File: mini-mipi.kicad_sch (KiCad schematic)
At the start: 0 parts

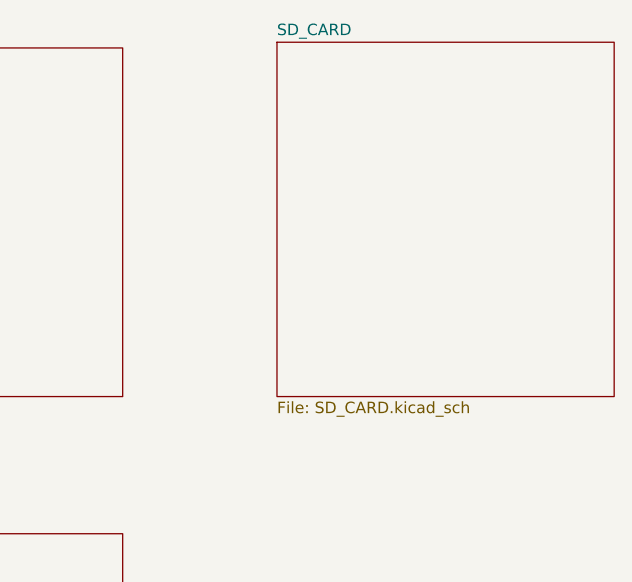
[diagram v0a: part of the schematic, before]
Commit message: Remove SD card, relocate regulators
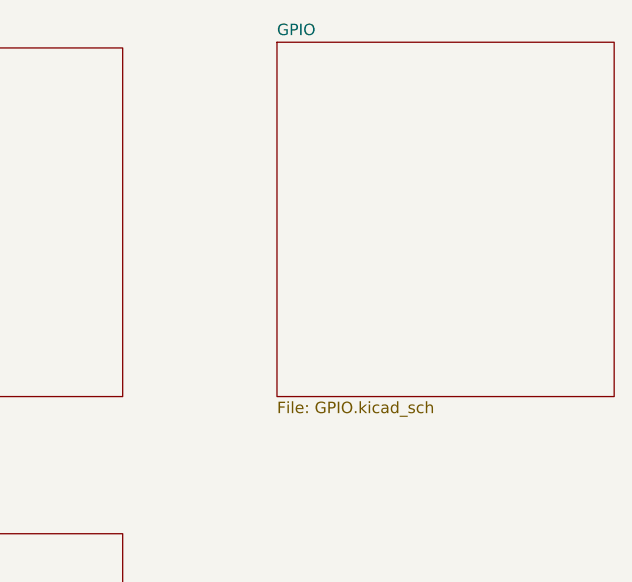
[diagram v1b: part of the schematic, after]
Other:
- sheet SD_CARD renamed GPIO
- sheet GPIO: file SD_CARD.kicad_sch -> GPIO.kicad_sch
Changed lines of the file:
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@@
-(kicad_sch (version 20200714) (host eeschema "5.99.0-unknown-8324cb3~102~ubuntu20.04.1")
+(kicad_sch (version 20200714) (host eeschema "5.99.0-unknown-027b6c8cf~102~ubuntu20.04.1")
   (page 1 6)
   (paper "A4")
@@
     )
   )
+  (sheet (at 207.645 43.18) (size 37.465 39.37)
+    (stroke (width 0.001) (type solid) (color 132 0 132 1))
+    (fill (color 255 255 255 0.0000))
+    (property "Sheet name" "GPIO" (id 0) (at 207.645 42.5441 0)
+      (effects (font (size 1.27 1.27)) (justify left bottom))
+    )
+    (property "Sheet file" "GPIO.kicad_sch" (id 1) (at 207.645 83.0589 0)
+      (effects (font (size 1.27 1.27)) (justify left top))
+    )
+  )
   (sheet (at 95.885 97.79) (size 34.925 29.845)
     (stroke (width 0.001) (type solid) (color 132 0 132 1))
@@
     )
   )
-  (sheet (at 207.645 43.18) (size 37.465 39.37)
-    (stroke (width 0.001) (type solid) (color 132 0 132 1))
-    (fill (color 255 255 255 0.0000))
-    (property "Sheet name" "SD_CARD" (id 0) (at 207.645 42.5441 0)
-      (effects (font (size 1.27 1.27)) (justify left bottom))
-    )
-    (property "Sheet file" "SD_CARD.kicad_sch" (id 1) (at 207.645 83.0589 0)
-      (effects (font (size 1.27 1.27)) (justify left top))
-    )
-  )
   (symbol_instances
     (path "/baa53bf9-daca-49ae-9e0d-ffb475a21435/898ad7f7-a0c6-4b72-8696-d86ef31c42ed"
@@
       (reference "#PWR0137") (unit 1)
     )
+    (path "/baa53bf9-daca-49ae-9e0d-ffb475a21435/310a54e5-8519-46fa-8e90-bd75a4f06582"
+      (reference "#PWR0151") (unit 1)
+    )
     (path "/baa53bf9-daca-49ae-9e0d-ffb475a21435/e369df8d-7bc0-4018-abea-2ddbb0b05648"
       (reference "C16") (unit 1)
@@
       (reference "C19") (unit 1)
     )
+    (path "/baa53bf9-daca-49ae-9e0d-ffb475a21435/9d904033-ab25-4a85-887c-bd0fbbf444d9"
+      (reference "C22") (unit 1)
+    )
     (path "/baa53bf9-daca-49ae-9e0d-ffb475a21435/70e6299b-b19c-469b-8113-15ef76301879"
       (reference "IC1") (unit 3)
@@
       (reference "#PWR0127") (unit 1)
     )
-    (path "/3f6b20e2-0af0-4e6d-a239-fbbb920f7ad3/efa53525-f126-4098-9bce-088c58985fd3"
+    (path "/3f6b20e2-0af0-4e6d-a239-fbbb920f7ad3/032a150b-85ae-4c68-ae3f-f4937bcc702e"
       (reference "#PWR0128") (unit 1)
     )
@@
       (reference "C2") (unit 1)
     )
-    (path "/3f6b20e2-0af0-4e6d-a239-fbbb920f7ad3/b2406567-d175-4f71-b4e4-c30e3317692d"
+    (path "/3f6b20e2-0af0-4e6d-a239-fbbb920f7ad3/b3910606-f8a0-414a-972a-a13f3f20bf6f"
       (reference "D1") (unit 1)
-    )
-    (path "/3f6b20e2-0af0-4e6d-a239-fbbb920f7ad3/4a8d2ba4-dd12-4599-94c3-38aad859b794"
-      (reference "D2") (unit 1)
     )
     (path "/3f6b20e2-0af0-4e6d-a239-fbbb920f7ad3/17ffadec-0811-496b-a0ce-0bdb99a7bf76"
@@
       (reference "R20") (unit 1)
     )
+    (path "/3f6b20e2-0af0-4e6d-a239-fbbb920f7ad3/b73fbf2e-397b-4acc-b296-438da13da3bd"
+      (reference "R25") (unit 1)
+    )
     (path "/3f6b20e2-0af0-4e6d-a239-fbbb920f7ad3/0f5c113f-b95a-4ea7-a5ce-136619995088"
       (reference "U5") (unit 1)
@@
       (reference "#PWR0143") (unit 1)
     )
+    (path "/8f541333-71c5-4e69-a5cb-3da6766b8bdb/e0b9767b-9f41-4b80-891c-0264532b6d01"
+      (reference "#PWR0144") (unit 1)
+    )
+    (path "/8f541333-71c5-4e69-a5cb-3da6766b8bdb/9f554b2f-50ba-43f3-8a86-bed4cf6888d8"
+      (reference "#PWR0145") (unit 1)
+    )
     (path "/8f541333-71c5-4e69-a5cb-3da6766b8bdb/cf33f7a9-1d66-4a4f-9f9d-875ef2fe3f53"
       (reference "#PWR0152") (unit 1)
     )
-    (path "/8f541333-71c5-4e69-a5cb-3da6766b8bdb/64b516fb-10fe-4eed-a6b3-0671c143f0c3"
+    (path "/8f541333-71c5-4e69-a5cb-3da6766b8bdb/dee2981e-1d47-4332-b5d3-443203db93db"
       (reference "C1") (unit 1)
     )
@@
       (reference "C21") (unit 1)
     )
-    (path "/8f541333-71c5-4e69-a5cb-3da6766b8bdb/abe4c710-cbf7-48f0-9c81-48d0620d8cc2"
-      (reference "C22") (unit 1)
+    (path "/8f541333-71c5-4e69-a5cb-3da6766b8bdb/e68f82e6-eb16-4452-8e5f-497090e7d4b3"
+      (reference "C23") (unit 1)
     )
     (path "/8f541333-71c5-4e69-a5cb-3da6766b8bdb/fce90540-fc92-43a8-b867-8ac57e0474f3"
@@
       (reference "U4") (unit 1)
     )
-    (path "/5523efa8-1e9d-4351-87af-f314779b18b2/7a782044-040e-460d-82d4-ef3de48d4bfa"
-      (reference "#PWR0144") (unit 1)
-    )
-    (path "/5523efa8-1e9d-4351-87af-f314779b18b2/b5b32cc7-35f1-4471-937d-464ddb649edb"
-      (reference "#PWR0145") (unit 1)
-    )
     (path "/5523efa8-1e9d-4351-87af-f314779b18b2/0c1108a7-3b2e-4732-9992-2e46badc2c13"
       (reference "#PWR0146") (unit 1)
@@
       (reference "IC1") (unit 2)
     )
-    (path "/5523efa8-1e9d-4351-87af-f314779b18b2/a4ed9e09-3784-4bf0-9aa8-77db411cd4cd"
-      (reference "J4") (unit 1)
-    )
     (path "/5523efa8-1e9d-4351-87af-f314779b18b2/e46f29f2-d303-41d2-afac-fefa34c62119"
